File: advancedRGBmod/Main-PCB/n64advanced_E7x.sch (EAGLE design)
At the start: 109 parts, among them J5 2510-, J6 UPS, U1 10CL010YE144, U2 ADV7125/ADV7123, U4 74LVC3G34, U5 S25FLXXXSO8-DUAL, U6 TLV70012DDC, U7 TLV70025DDC

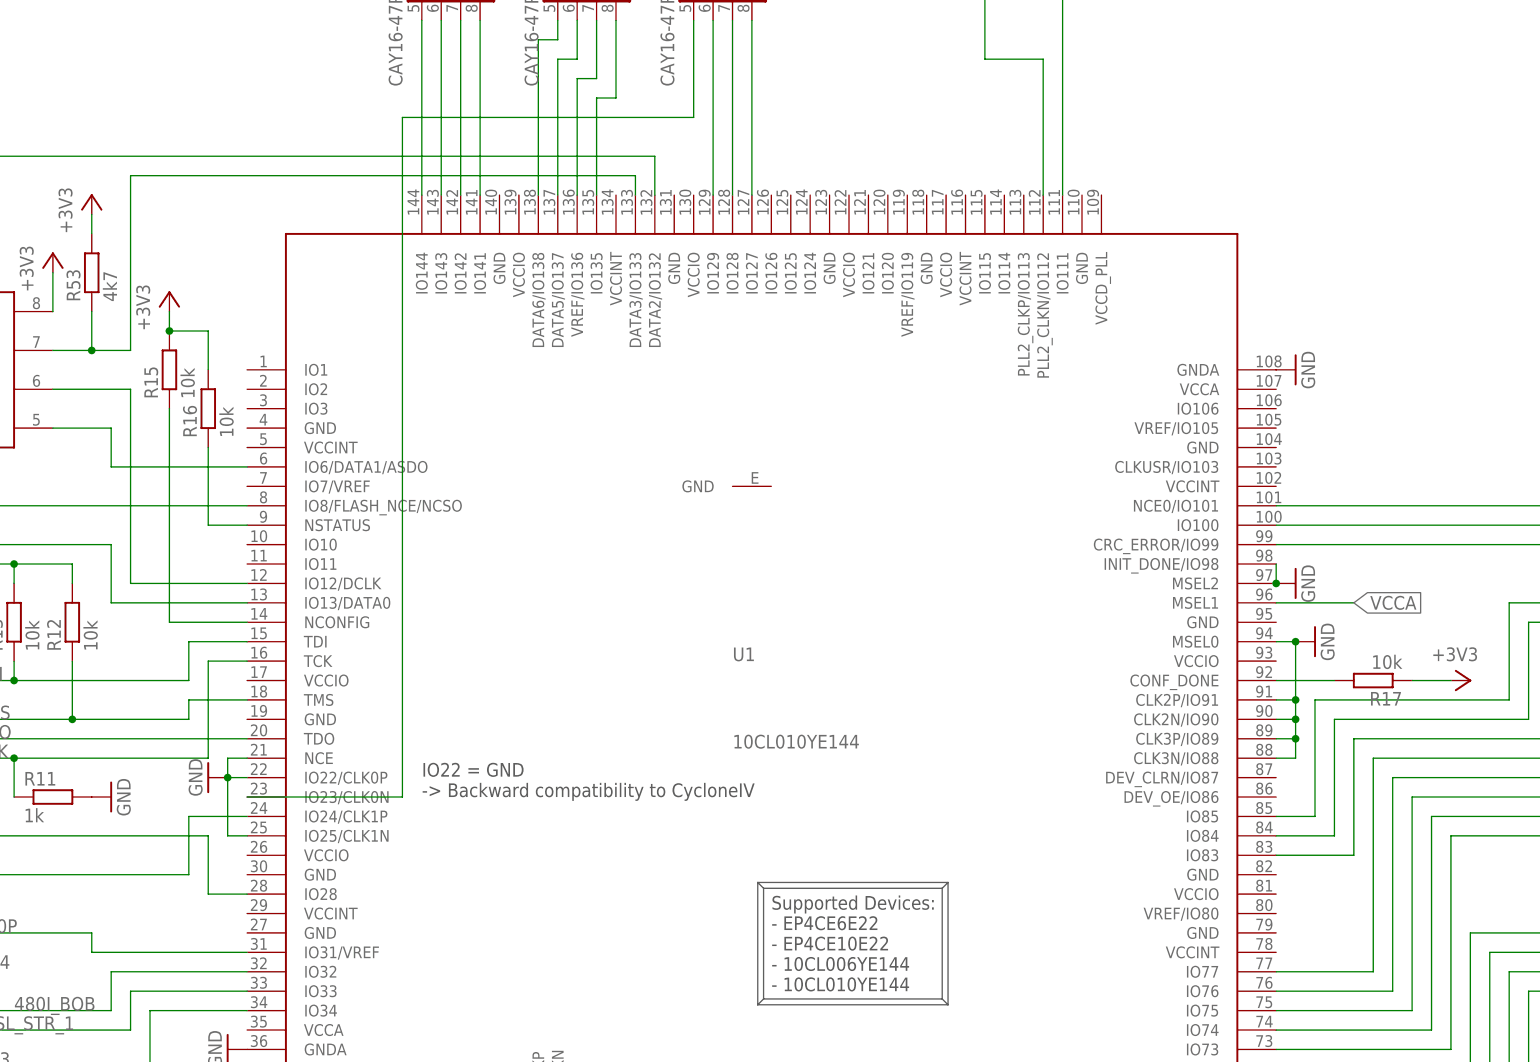
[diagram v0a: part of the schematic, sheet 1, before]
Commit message: PCB Update: - unused VREF to VCCIO (see connection guideline) - unused DEV_CLRn and DEV_OE to GND (see connection guideline) - rename of some resistors
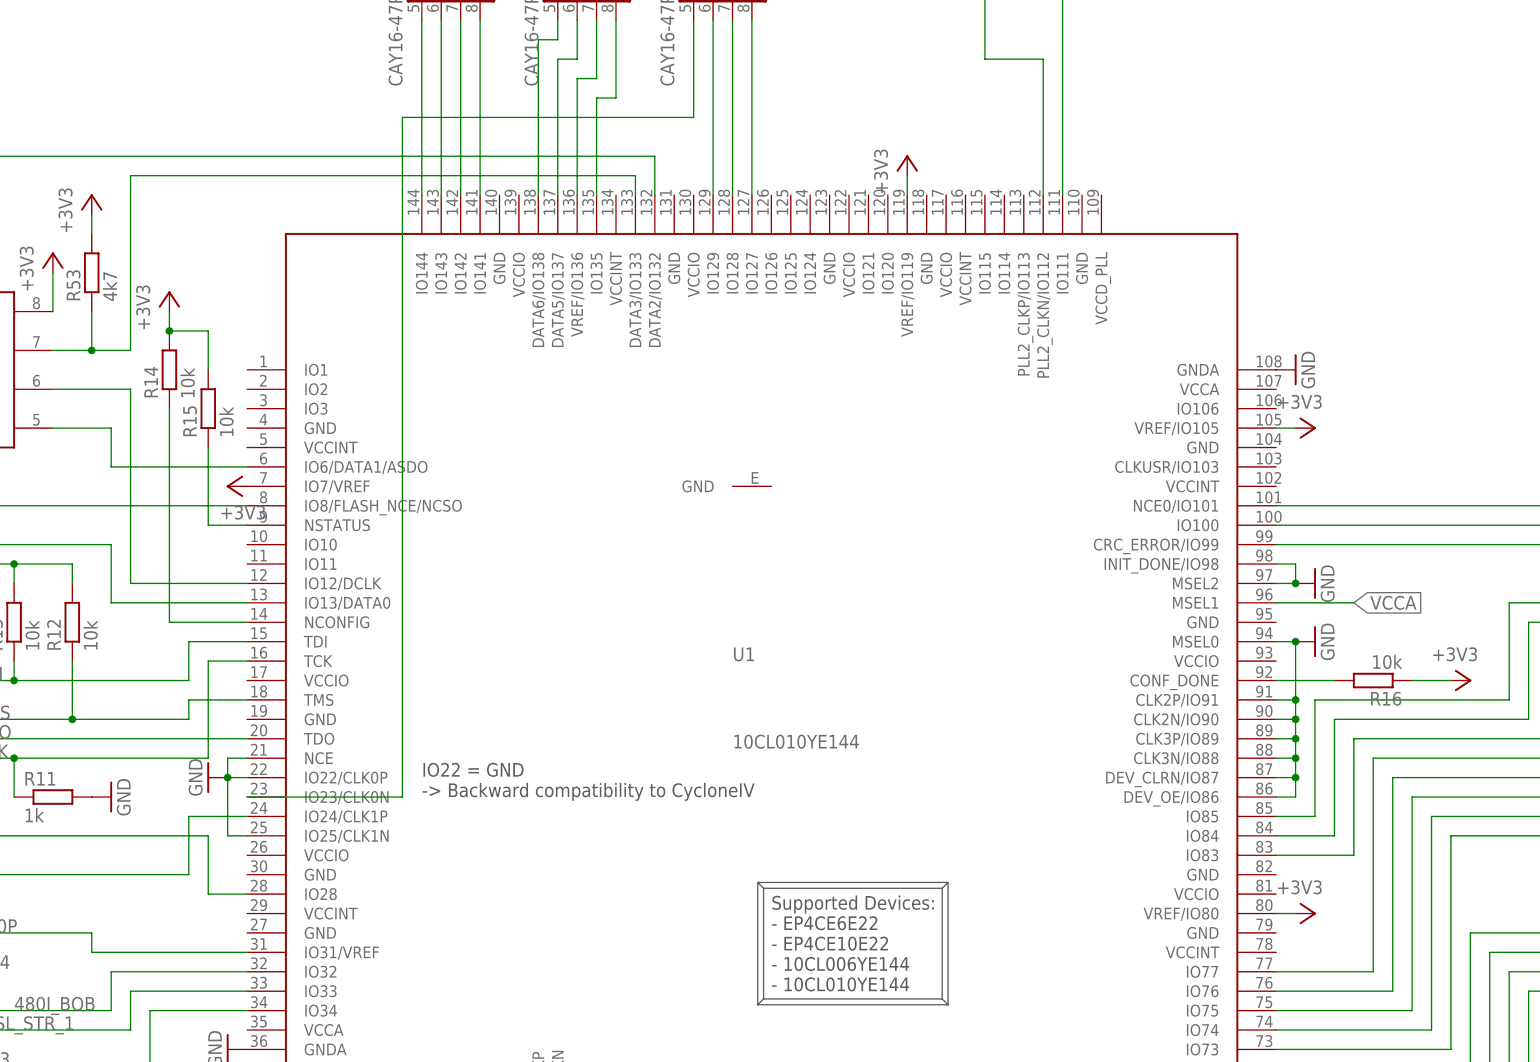
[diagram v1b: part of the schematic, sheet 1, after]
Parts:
- removed R17: 10k, rcl:R-EU_R0603
- added R14: 10k, rcl:R-EU_R0603
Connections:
- net GND: now also U1.DEV_CLRN/IO87, U1.DEV_OE/IO86
- net N$45: now also R15.1; no longer R16.1
- net N$52: now also R16.2; no longer R17.2
- net N$8: now also R14.1; no longer R15.1
- net VCCIO: now also R14.2, R16.1, U1.IO7/VREF, U1.VREF/IO105, U1.VREF/IO119, U1.VREF/IO80; no longer R16.2, R17.1
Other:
- moved on the sheet: R15, R16
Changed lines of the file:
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@@
 <part name="J4" library="jumper" deviceset="SJ2W" device=""/>
 <part name="J6" library="jumper" deviceset="SJ" device="" value="UPS"/>
-<part name="R15" library="rcl" deviceset="R-EU_" device="R0603" value="10k"/>
+<part name="R14" library="rcl" deviceset="R-EU_" device="R0603" value="10k"/>
 <part name="AGND17" library="supply1" deviceset="GND" device=""/>
 <part name="AGND18" library="supply1" deviceset="GND" device=""/>
 <part name="AGND19" library="supply1" deviceset="GND" device=""/>
-<part name="R17" library="rcl" deviceset="R-EU_" device="R0603" value="10k"/>
+<part name="R16" library="rcl" deviceset="R-EU_" device="R0603" value="10k"/>
 <part name="+3V27" library="supply1" deviceset="+3V3" device=""/>
-<part name="R16" library="rcl" deviceset="R-EU_" device="R0603" value="10k"/>
+<part name="R15" library="rcl" deviceset="R-EU_" device="R0603" value="10k"/>
 <part name="GND5" library="supply1" deviceset="GND" device=""/>
 <part name="J2" library="jumper" deviceset="SJ2W" device=""/>
@@
 <part name="GND2" library="supply1@1" deviceset="GND" device=""/>
 <part name="+3V5" library="supply1" deviceset="+3V3" device=""/>
+<part name="+3V6" library="supply1" deviceset="+3V3" device=""/>
+<part name="+3V10" library="supply1" deviceset="+3V3" device=""/>
+<part name="+3V11" library="supply1" deviceset="+3V3" device=""/>
+<part name="+3V12" library="supply1" deviceset="+3V3" device=""/>
 </parts>
 <sheets>
@@
 <instance part="RN41" gate="G$1" x="309.88" y="187.96"/>
 <instance part="J4" gate="G$1" x="43.18" y="66.04"/>
-<instance part="R15" gate="G$1" x="68.58" y="144.78" rot="R90"/>
+<instance part="R14" gate="G$1" x="68.58" y="144.78" rot="R90"/>
 <instance part="AGND17" gate="1" x="256.54" y="76.2" rot="R270"/>
 <instance part="AGND18" gate="1" x="302.26" y="101.6" rot="R180"/>
 <instance part="AGND19" gate="1" x="287.02" y="25.4"/>
-<instance part="R17" gate="G$1" x="226.06" y="104.14" rot="R180"/>
+<instance part="R16" gate="G$1" x="226.06" y="104.14" rot="R180"/>
 <instance part="+3V27" gate="G$1" x="68.58" y="154.94"/>
-<instance part="R16" gate="G$1" x="73.66" y="139.7" rot="R90"/>
+<instance part="R15" gate="G$1" x="73.66" y="139.7" rot="R90"/>
 <instance part="J2" gate="G$1" x="43.18" y="40.64"/>
 <instance part="U4" gate="G$1" x="281.94" y="203.2"/>
@@
 <instance part="R51" gate="G$1" x="20.32" y="121.92"/>
 <instance part="R53" gate="G$1" x="58.42" y="157.48" rot="R90"/>
-<instance part="GND19" gate="1" x="215.9" y="116.84" rot="R90"/>
+<instance part="GND19" gate="1" x="218.44" y="116.84" rot="R90"/>
 <instance part="GND20" gate="1" x="218.44" y="109.22" rot="R90"/>
 <instance part="+3V9" gate="G$1" x="238.76" y="104.14" rot="R270"/>
@@
 <instance part="GND2" gate="1" x="17.78" y="134.62"/>
 <instance part="+3V5" gate="G$1" x="58.42" y="167.64"/>
+<instance part="+3V6" gate="G$1" x="76.2" y="129.54" rot="R90"/>
+<instance part="+3V10" gate="G$1" x="218.44" y="73.66" rot="R270"/>
+<instance part="+3V11" gate="G$1" x="218.44" y="137.16" rot="R270"/>
+<instance part="+3V12" gate="G$1" x="165.1" y="172.72"/>
 </instances>
 <busses>
@@
 <pinref part="GND19" gate="1" pin="GND"/>
 <pinref part="U1" gate="G$1" pin="INIT_DONE/IO98"/>
-<wire x1="213.36" y1="119.38" x2="213.36" y2="116.84" width="0.1524" layer="91"/>
-<junction x="213.36" y="116.84"/>
+<junction x="215.9" y="116.84"/>
+<wire x1="215.9" y1="116.84" x2="213.36" y2="116.84" width="0.1524" layer="91"/>
+<wire x1="213.36" y1="119.38" x2="215.9" y2="119.38" width="0.1524" layer="91"/>
+<wire x1="215.9" y1="119.38" x2="215.9" y2="116.84" width="0.1524" layer="91"/>
 </segment>
 <segment>
@@
 <wire x1="215.9" y1="93.98" x2="215.9" y2="96.52" width="0.1524" layer="91"/>
 <junction x="215.9" y="96.52"/>
+<pinref part="U1" gate="G$1" pin="DEV_CLRN/IO87"/>
+<wire x1="213.36" y1="91.44" x2="215.9" y2="91.44" width="0.1524" layer="91"/>
+<wire x1="215.9" y1="91.44" x2="215.9" y2="93.98" width="0.1524" layer="91"/>
+<junction x="215.9" y="93.98"/>
+<pinref part="U1" gate="G$1" pin="DEV_OE/IO86"/>
+<wire x1="213.36" y1="88.9" x2="215.9" y2="88.9" width="0.1524" layer="91"/>
+<wire x1="215.9" y1="88.9" x2="215.9" y2="91.44" width="0.1524" layer="91"/>
+<junction x="215.9" y="91.44"/>
 </segment>
 <segment>
@@
 </segment>
 <segment>
-<pinref part="R17" gate="G$1" pin="1"/>
+<pinref part="R16" gate="G$1" pin="1"/>
 <pinref part="+3V9" gate="G$1" pin="+3V3"/>
 <wire x1="231.14" y1="104.14" x2="236.22" y2="104.14" width="0.1524" layer="91"/>
@@
 <segment>
 <pinref part="+3V27" gate="G$1" pin="+3V3"/>
+<pinref part="R14" gate="G$1" pin="2"/>
+<wire x1="68.58" y1="152.4" x2="68.58" y2="149.86" width="0.1524" layer="91"/>
 <pinref part="R15" gate="G$1" pin="2"/>
-<wire x1="68.58" y1="152.4" x2="68.58" y2="149.86" width="0.1524" layer="91"/>
-<pinref part="R16" gate="G$1" pin="2"/>
 <wire x1="73.66" y1="144.78" x2="73.66" y2="149.86" width="0.1524" layer="91"/>
 <wire x1="73.66" y1="149.86" x2="68.58" y2="149.86" width="0.1524" layer="91"/>
@@
 <pinref part="+3V8" gate="G$1" pin="+3V3"/>
 <wire x1="7.62" y1="160.02" x2="7.62" y2="157.48" width="0.1524" layer="91"/>
+</segment>
+<segment>
+<pinref part="U1" gate="G$1" pin="IO7/VREF"/>
+<pinref part="+3V6" gate="G$1" pin="+3V3"/>
+</segment>
+<segment>
+<wire x1="213.36" y1="73.66" x2="215.9" y2="73.66" width="0.1524" layer="91"/>
+<pinref part="U1" gate="G$1" pin="VREF/IO80"/>
+<pinref part="+3V10" gate="G$1" pin="+3V3"/>
+</segment>
+<segment>
+<wire x1="213.36" y1="137.16" x2="215.9" y2="137.16" width="0.1524" layer="91"/>
+<pinref part="U1" gate="G$1" pin="VREF/IO105"/>
+<pinref part="+3V11" gate="G$1" pin="+3V3"/>
+</segment>
+<segment>
+<wire x1="165.1" y1="167.64" x2="165.1" y2="170.18" width="0.1524" layer="91"/>
+<pinref part="U1" gate="G$1" pin="VREF/IO119"/>
+<pinref part="+3V12" gate="G$1" pin="+3V3"/>
 </segment>
 </net>
@@
 <segment>
 <pinref part="U1" gate="G$1" pin="CONF_DONE"/>
-<pinref part="R17" gate="G$1" pin="2"/>
+<pinref part="R16" gate="G$1" pin="2"/>
 <wire x1="213.36" y1="104.14" x2="220.98" y2="104.14" width="0.1524" layer="91"/>
 </segment>
@@
 <segment>
 <pinref part="U1" gate="G$1" pin="NSTATUS"/>
-<pinref part="R16" gate="G$1" pin="1"/>
+<pinref part="R15" gate="G$1" pin="1"/>
 <wire x1="78.74" y1="124.46" x2="73.66" y2="124.46" width="0.1524" layer="91"/>
 <wire x1="73.66" y1="124.46" x2="73.66" y2="134.62" width="0.1524" layer="91"/>
@@
 <segment>
 <pinref part="U1" gate="G$1" pin="NCONFIG"/>
-<pinref part="R15" gate="G$1" pin="1"/>
+<pinref part="R14" gate="G$1" pin="1"/>
 <wire x1="78.74" y1="111.76" x2="68.58" y2="111.76" width="0.1524" layer="91"/>
 <wire x1="68.58" y1="111.76" x2="68.58" y2="139.7" width="0.1524" layer="91"/>

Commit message: important BOM update: Use Schmitt triggered buffer instead of simple one!!!
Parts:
- U4: value 74LVC3G34 -> 74LVC3G17
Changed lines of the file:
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@@
 <part name="GND5" library="supply1" deviceset="GND" device=""/>
 <part name="J2" library="jumper" deviceset="SJ2W" device=""/>
-<part name="U4" library="OSSC_HDMI_Audio" deviceset="74LVC3G34" device=""/>
+<part name="U4" library="OSSC_HDMI_Audio" deviceset="74LVC3G34" device="" value="74LVC3G17"/>
 <part name="C401" library="rcl" deviceset="C-EU" device="C0603" value="0.1u"/>
 <part name="P+8" library="supply1" deviceset="+5V" device=""/>

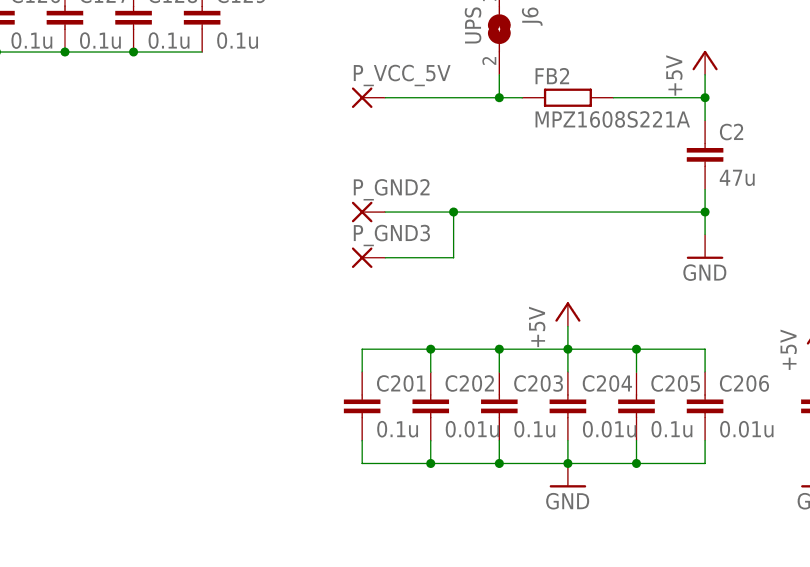
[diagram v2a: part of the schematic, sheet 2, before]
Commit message: Update PCB - reroute power supply layer reducing noise injection to +5V plane from digital signals - adapt some component positions
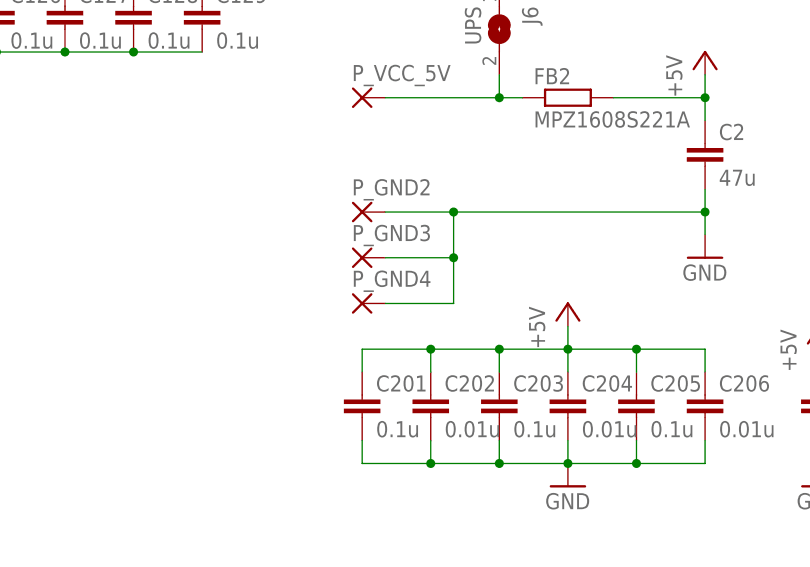
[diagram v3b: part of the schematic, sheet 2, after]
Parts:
- added P_GND4: (no value), wirepad@1:SMD2
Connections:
- net GND: now also P_GND4.P
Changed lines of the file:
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@@
 <part name="+3V11" library="supply1" deviceset="+3V3" device=""/>
 <part name="+3V12" library="supply1" deviceset="+3V3" device=""/>
+<part name="P_GND4" library="wirepad@1" deviceset="SMD2" device=""/>
 </parts>
 <sheets>
@@
 <instance part="C801" gate="G$1" x="208.28" y="93.98"/>
 <instance part="FB4" gate="G$1" x="193.04" y="96.52"/>
+<instance part="P_GND4" gate="1" x="154.94" y="33.02"/>
 </instances>
 <busses>
@@
 <wire x1="193.04" y1="45.72" x2="193.04" y2="43.18" width="0.1524" layer="91"/>
 <junction x="193.04" y="43.18"/>
-</segment>
-<segment>
+<pinref part="P_GND4" gate="1" pin="P"/>
+<wire x1="157.48" y1="33.02" x2="165.1" y2="33.02" width="0.1524" layer="91"/>
+<wire x1="165.1" y1="33.02" x2="165.1" y2="38.1" width="0.1524" layer="91"/>
+<junction x="165.1" y="38.1"/>
+</segment>
+<segment>
